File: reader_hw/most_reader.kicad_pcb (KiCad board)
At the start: 2 copper layers, 106 x 90 mm, 58 parts, among them J1 1-1394640-1, J4 VBAT_IN, J6 PLT133/T10W, M1 Tang Nano 20K, U1 74LVC1G34, U3 74LVC1G125, U4 74LVC1G123, U5 TPS7B8133DRV, U6 LMR38020F

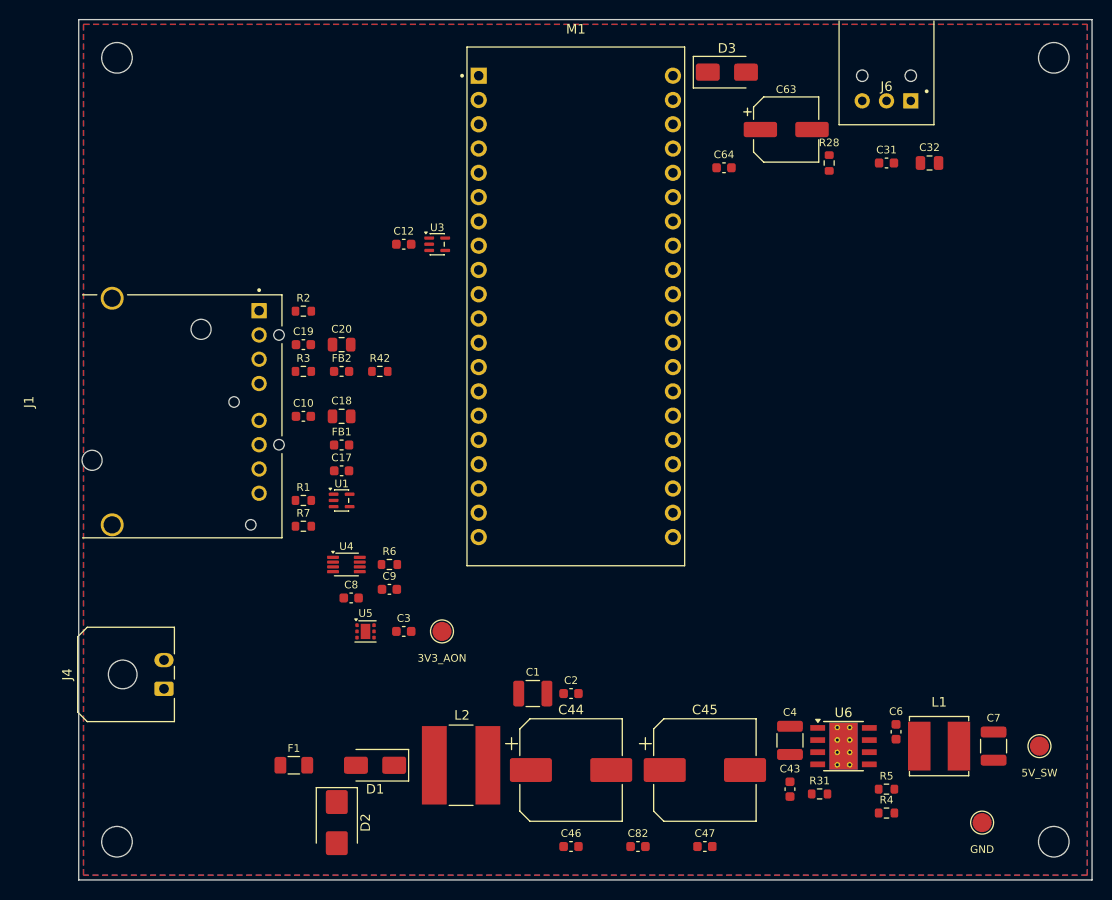
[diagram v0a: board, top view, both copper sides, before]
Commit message: Step 2, the board routed: the user's placement, 77.54 x 55.55 mm, no jumper
The layout is the board's own, not the listener's cut down. The user re-placed it six
times on 2026-10-03 and cut 6.45 mm off the top. gen_reader_pcb.py's PLACE, REFPOS and
TPTEXT now hold that placement, read back off the board, and --fresh on a copy lays
every part where the board has it.

Routing follows the listener's scheme. Every signal and supply runs on the top. The
bottom is one unbroken ground plane with nothing but vias in it. The top pour is
stitched every 6 mm, and every SMD ground pad has its own via.
- The ring: RXD 4 mm from J1 to R1/U1, TXD up a lane to J1 pin 1, RX_BUF through U1's
  and U3's bodies to the FPGA's pin 27, its branch to U4 between J1's pins 5 and 6.
- 3V3_AON from U5 under J1's body into FB2 and FB1.
- VBAT_P under the module to the buck.
- 5 V up the right edge to C63, C85, C64 and D3.
- No signal within 3.5 mm of a mounting hole's centre: TXD bends away from H1, S/PDIF
  goes round H2.

The sheet, from the user's edits:
- C83 (100 nF, 100 V) moves across the input behind F1, beside D2.
- C84 (100 V) on the VBAT_P riser.
- C85 on 5V_SW.
- TP10, a second ground test point.
- 3V3_SW, the supply of U3 and J6, now comes from module pin 7 (FPGA pin 16, LED1,
  held high by the gateware: U3 takes microamps, J6 3 mA, 10 at most), not pin 19.
  Pin 7 sits above /WAKE, so the last jumper is gone. The module's own 3.3 V pins are
  not wired.

The board carries a title block: JLR MOST reader, rev 1.0, 2026-10-03.

Checks: DRC 0 violations, 0 unconnected, 0 differences from the sheet. ERC 0/0.
check_sheet PASS. Tracks 558 mm, all on the top; 155 vias, all ground.

Co-Authored-By: Claude Opus 5.5 <noreply@anthropic.com>
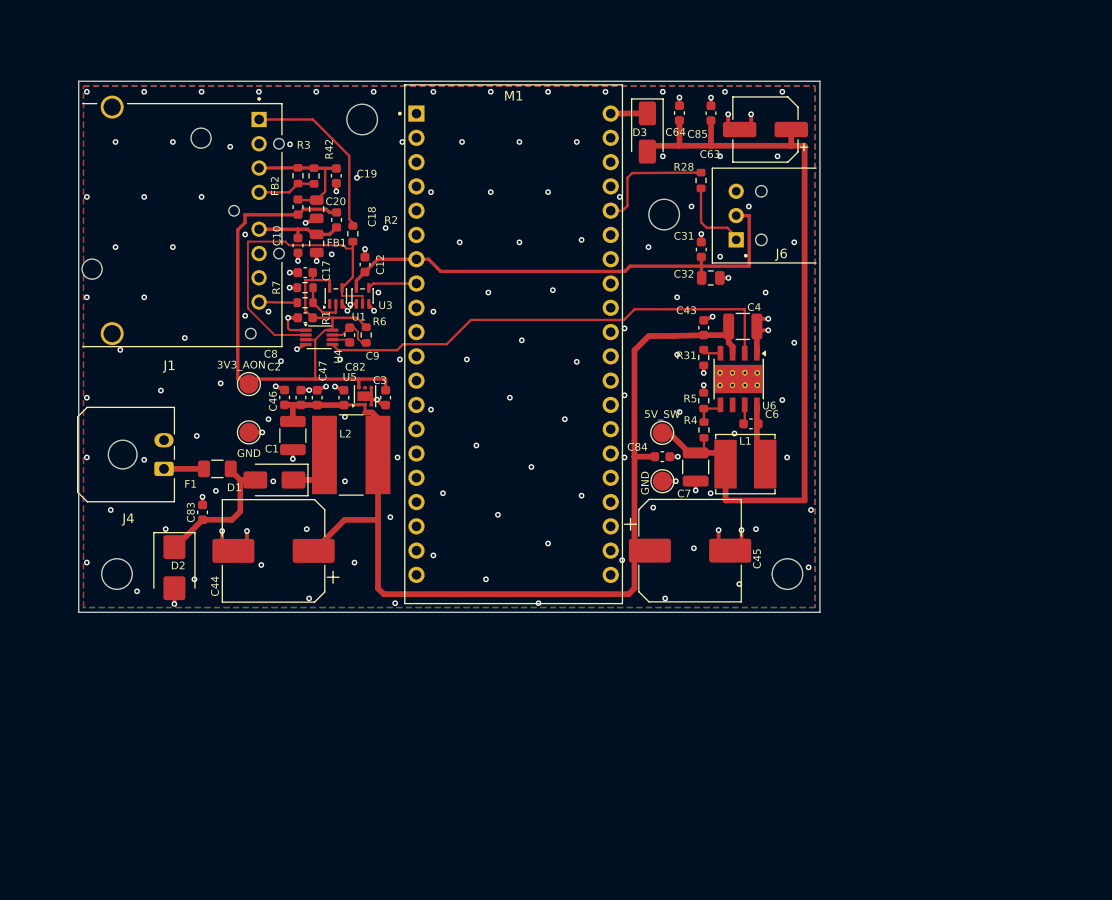
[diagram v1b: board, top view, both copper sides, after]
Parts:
- added C83: 100n 100V, Capacitor_SMD:C_0603_1608Metric, F.Cu at (13.0, 51.5)
- added C84: 100n 100V, Capacitor_SMD:C_0603_1608Metric, F.Cu at (61.0, 45.7)
- added C85: 100n, Capacitor_SMD:C_0603_1608Metric, F.Cu at (66.1, 9.79)
- added TP10: GND, TestPoint:TestPoint_Pad_D2.0mm, F.Cu at (17.8, 43.2)
- moved C47 62.0 mm to (24.9, 39.5), turned to 90 degrees
- moved C82 56.1 mm to (27.7, 39.5), turned to 90 degrees
- moved C46 55.7 mm to (21.5, 39.5), turned to 90 degrees
- moved TP7 51.3 mm to (61.0, 43.2)
- moved C43 49.1 mm to (65.4, 32.2)
- moved TP9 48.9 mm to (61.1, 48.3)
- moved R31 47.2 mm to (65.4, 35.3), turned to 90 degrees
- moved R5 44.9 mm to (65.4, 39.9), turned to 90 degrees
- moved R4 44.4 mm to (65.4, 42.9), turned to 90 degrees
- moved H2 43.9 mm to (61.2, 20.4)
- moved C4 43.6 mm to (69.5, 32.1), turned to 0 degrees
- moved C7 42.7 mm to (64.5, 46.8), turned to -90 degrees
- moved C2 41.9 mm to (23.2, 39.5), turned to 90 degrees
- moved U6 39.9 mm to (69.0, 37.6), turned to -90 degrees
- moved H4 39.5 mm to (74.1, 58.0)
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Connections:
- M1 pad 19: 3V3_SW -> unconnected-(M1-3V3-Pad19)
- M1 pad 7: unconnected-(M1-16_LED1-Pad7) -> 3V3_SW
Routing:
- net VBAT_P: track 0.00 -> 98.6 mm
- net 5V_SW: track 0.00 -> 79.5 mm
- net 3V3_AON: track 0.00 -> 68.6 mm
- net 3V3_SW: track 0.00 -> 52.4 mm
- net /WAKE: track 0.00 -> 49.7 mm
- net GND: track 0.00 -> 47.3 mm, vias 0 -> 155
- net /RX_BUF: track 0.00 -> 34.6 mm
- net Net-(J1-TXD): track 0.00 -> 18.5 mm
- net Net-(D1-A): track 0.00 -> 15.0 mm
- net Net-(J1-TXVCC): track 0.00 -> 13.7 mm
- net /SPDIF_F: track 0.00 -> 12.8 mm
- net Net-(J1-RXVCC): track 0.00 -> 9.55 mm
- net Net-(J6-VIN): track 0.00 -> 8.18 mm
- net Net-(J1-RGAIN): track 0.00 -> 6.12 mm
- net Net-(U1-A): track 0.00 -> 5.30 mm
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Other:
- board size 106 x 90 mm -> 77.5 x 55.5 mm
